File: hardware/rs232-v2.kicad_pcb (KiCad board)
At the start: 2 copper layers, 45 x 35 mm, 37 parts, among them J1 DB9, P1 CON-SENSOR, P2 CONN_5, P3 CONN_5, P4 BOOT, P5 BOOT, U1 XMC1404, U3 SP3232EBCN, U4 DRILL, U5 DRILL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

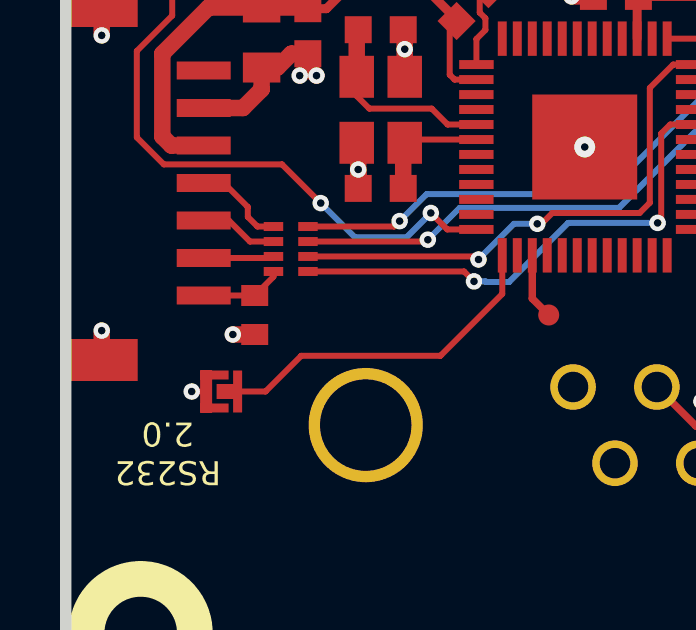
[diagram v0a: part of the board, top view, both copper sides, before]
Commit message: Change capacitor footprint(s) to C0402F
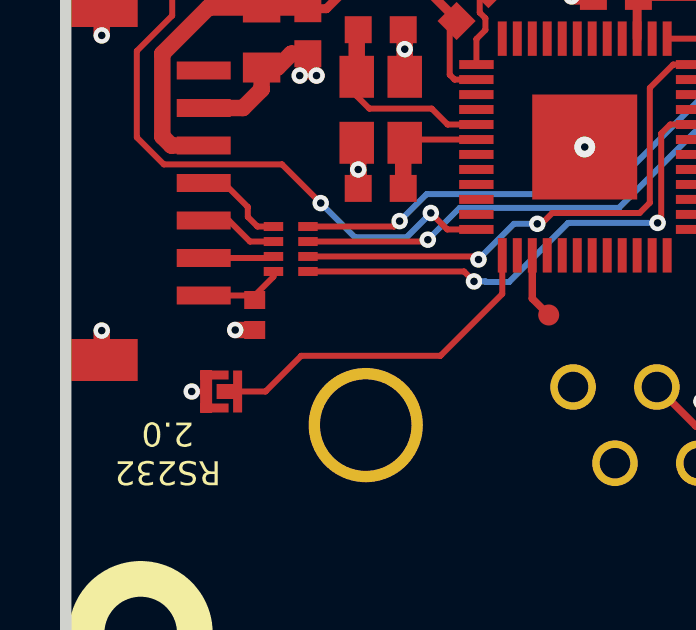
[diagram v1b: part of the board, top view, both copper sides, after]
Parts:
- C1: footprint kicad-libraries:C0402E -> kicad-libraries:C0402F
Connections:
- J1 pad 2: (no net) -> Net-(J1-Pad2)
- J1 pad 5: (no net) -> Net-(J1-Pad5)
- J1 pad 6: (no net) -> Net-(J1-Pad6)
- J1 pad 9: (no net) -> Net-(J1-Pad9)
- P1 pad 1: (no net) -> Net-(P1-Pad1)
- U1 pad 10: (no net) -> Net-(U1-Pad10)
- U1 pad 11: (no net) -> Net-(U1-Pad11)
- U1 pad 12: (no net) -> Net-(U1-Pad12)
- U1 pad 2: (no net) -> Net-(U1-Pad2)
- U1 pad 21: (no net) -> Net-(U1-Pad21)
- U1 pad 22: (no net) -> Net-(U1-Pad22)
- U1 pad 26: (no net) -> Net-(U1-Pad26)
- U1 pad 28: (no net) -> Net-(U1-Pad28)
- U1 pad 29: (no net) -> Net-(U1-Pad29)
- U1 pad 30: (no net) -> Net-(U1-Pad30)
- U1 pad 31: (no net) -> Net-(U1-Pad31)
- U1 pad 32: (no net) -> Net-(U1-Pad32)
- U1 pad 33: (no net) -> Net-(U1-Pad33)
- U1 pad 34: (no net) -> Net-(U1-Pad34)
- U1 pad 35: (no net) -> Net-(U1-Pad35)
- U1 pad 36: (no net) -> Net-(U1-Pad36)
- U1 pad 39: (no net) -> Net-(U1-Pad39)
- U1 pad 4: (no net) -> Net-(U1-Pad4)
- U1 pad 40: (no net) -> Net-(U1-Pad40)
- U1 pad 43: (no net) -> Net-(U1-Pad43)
- U1 pad 44: (no net) -> Net-(U1-Pad44)
- U1 pad 45: (no net) -> Net-(U1-Pad45)
- U1 pad 46: (no net) -> Net-(U1-Pad46)
- U1 pad 47: (no net) -> Net-(U1-Pad47)
- U1 pad 5: (no net) -> Net-(U1-Pad5)
- U1 pad 6: (no net) -> Net-(U1-Pad6)
- U1 pad 7: (no net) -> Net-(U1-Pad7)
- U1 pad 8: (no net) -> Net-(U1-Pad8)
- U1 pad 9: (no net) -> Net-(U1-Pad9)

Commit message: fix library, define xmc1403 as minimum instead of xmc1404
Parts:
- U1: value XMC1404 -> XMC1403
